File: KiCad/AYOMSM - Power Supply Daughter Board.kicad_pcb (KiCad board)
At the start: 2 copper layers, 97.8 x 47.3 mm, 21 parts

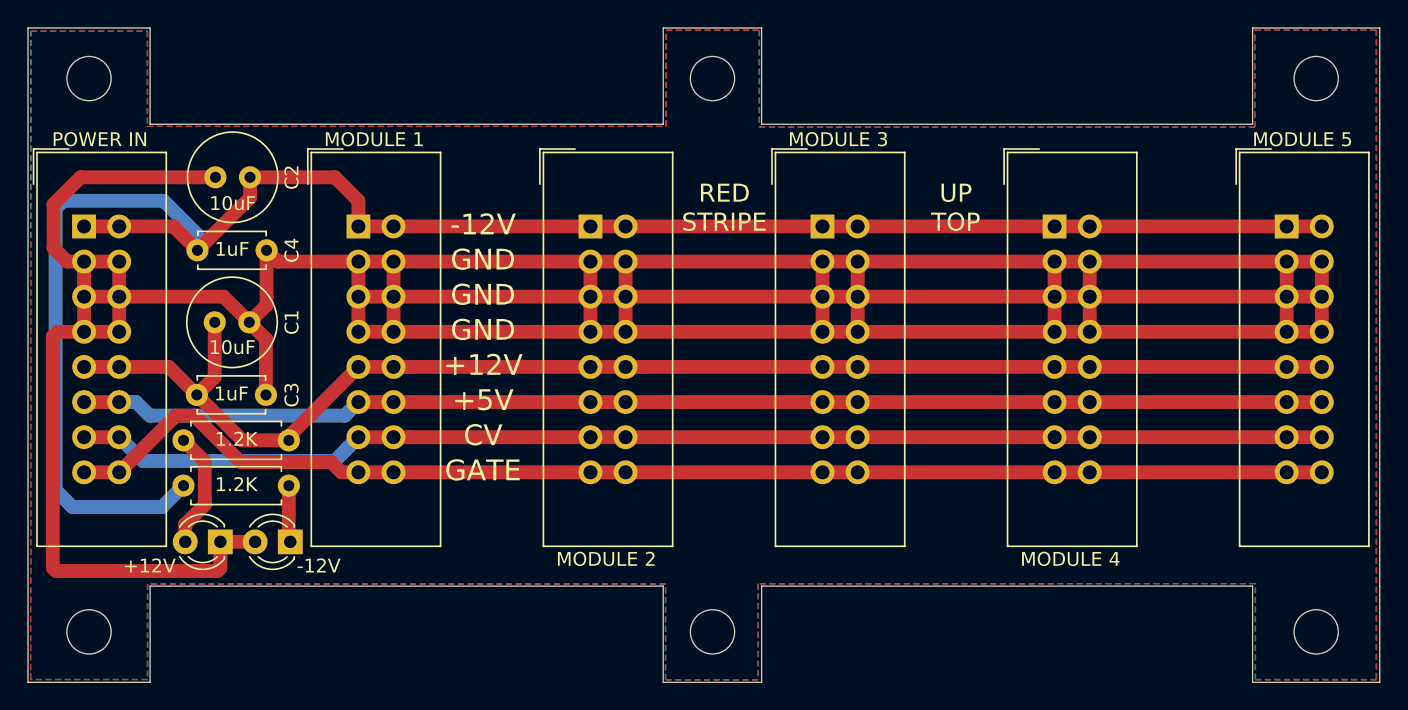
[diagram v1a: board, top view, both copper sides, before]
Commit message: Added 10-pin Power-In connector, updated layout
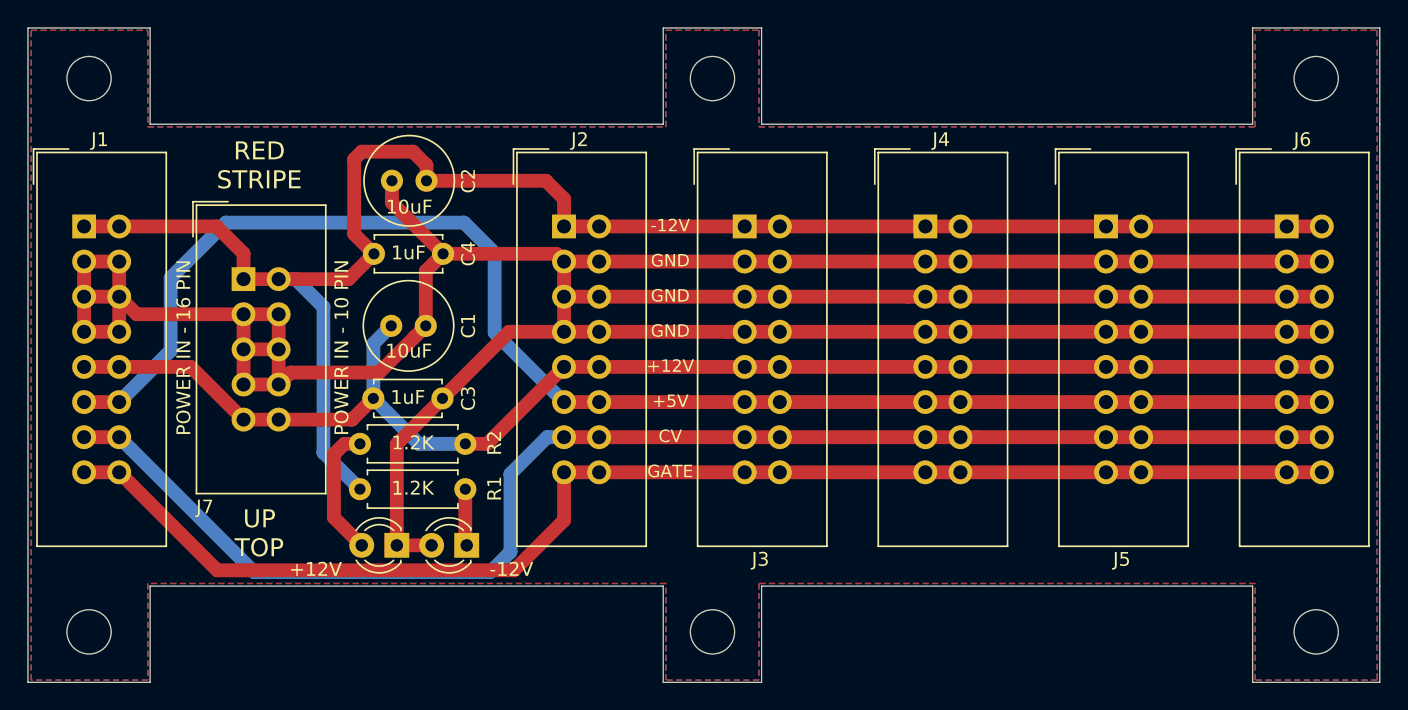
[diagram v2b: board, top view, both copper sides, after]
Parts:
- added J7: PWR_IN_10, Connector_IDC:IDC-Header_2x05_P2.54mm_Vertical, F.Cu at (124.6, 72.5)
- J1: renamed from POWER IN
- J2: renamed from MODULE 1
- J3: renamed from MODULE 2
- J4: renamed from MODULE 3
- J5: renamed from MODULE 4
- J6: renamed from MODULE 5
- moved G*** 35.9 mm to (123.3, 84.6)
- moved J2 14.9 mm to (147.8, 68.7)
- moved R1 12.8 mm to (140.6, 87.7)
- moved R2 12.8 mm to (133.0, 84.5)
- moved +12V 12.8 mm to (135.7, 91.8)
- moved -12V 12.8 mm to (140.7, 91.8)
- moved C2 12.8 mm to (135.3, 65.4)
- moved C3 12.8 mm to (134.0, 81.2)
- moved C4 12.8 mm to (139.0, 70.7)
- moved C1 12.8 mm to (135.3, 75.9)
- moved J3 11.2 mm to (160.8, 68.7)
- moved J4 7.44 mm to (173.9, 68.7)
- moved J5 3.72 mm to (187.0, 68.7)
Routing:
- net GND: track 360.4 -> 273.8 mm
- net /5V: track 90.3 -> 106.7 mm
- net -12V: track 139.2 -> 124.4 mm
- net /CV: track 90.9 -> 100.9 mm
- net /GATE: track 92.9 -> 97.4 mm
- net +12V: track 99.9 -> 101.2 mm
- net Net-(D1-Pad2): track 8.57 -> 9.61 mm
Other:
- board text added: "POWER IN - 10 PIN"
- board text added: "POWER IN - 16 PIN"
- board text added: "R1"
- board text added: "R2"
- board text added: "Shapetaker - Power Supply Daughter Board (Power Bus - Rev 1.1)"
- board text removed: "Shapetaker - Power Supply Daughter Board (Power Bus - Rev 1.0)"

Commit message: Updated BOM, ordering information, updated silkscreen, added README
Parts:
- renumbered +12V to D1, -12V to D2
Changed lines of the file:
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@@
   (general
     (thickness 1.6)
-    (drawings 37)
+    (drawings 41)
     (tracks 167)
     (zones 0)
@@
   )
   (page A4)
+  (title_block
+    (title "Power Supply Bus")
+    (date 2020-07-25)
+    (rev 1.0)
+    (company Shapetaker)
+  )
   (layers
     (0 F.Cu signal)
@@
     (descr "LED, diameter 3.0mm, 2 pins")
     (tags "LED diameter 3.0mm 2 pins")
-    (fp_text reference +12V (at 5.8801 -1.7399) (layer F.SilkS)
+    (fp_text reference D1 (at 4.6736 -2.1209) (layer F.SilkS)
       (effects (font (size 1 1) (thickness 0.15)))
     )
@@
     (descr "LED, diameter 3.0mm, 2 pins")
     (tags "LED diameter 3.0mm 2 pins")
-    (fp_text reference -12V (at -3.2258 -1.7399) (layer F.SilkS)
+    (fp_text reference D2 (at -2.2098 -2.1209) (layer F.SilkS)
       (effects (font (size 1 1) (thickness 0.15)))
     )
@@
     )
   )
-  (gr_text R2 (at 142.748 84.3915 90) (layer F.SilkS)
+  (gr_text -12V (at 143.006 90.551 270) (layer F.SilkS)
     (effects (font (size 1 1) (thickness 0.15)))
   )
-  (gr_text R1 (at 142.748 87.6935 90) (layer F.SilkS)
+  (gr_text +12V (at 131.0045 90.551 270) (layer F.SilkS)
     (effects (font (size 1 1) (thickness 0.15)))
   )
-  (gr_text "POWER IN - 10 PIN" (at 131.699 77.497401 90) (layer F.SilkS)
+  (dimension 47.3202 (width 0.15) (layer Dwgs.User)
+    (gr_text "47.320 mm" (at 103.7925 78.0415 270) (layer Dwgs.User)
+      (effects (font (size 1 1) (thickness 0.15)))
+    )
+    (feature1 (pts (xy 109 101.7016) (xy 104.506079 101.7016)))
+    (feature2 (pts (xy 109 54.3814) (xy 104.506079 54.3814)))
+    (crossbar (pts (xy 105.0925 54.3814) (xy 105.0925 101.7016)))
+    (arrow1a (pts (xy 105.0925 101.7016) (xy 104.506079 100.575096)))
+    (arrow1b (pts (xy 105.0925 101.7016) (xy 105.678921 100.575096)))
+    (arrow2a (pts (xy 105.0925 54.3814) (xy 104.506079 55.507904)))
+    (arrow2b (pts (xy 105.0925 54.3814) (xy 105.678921 55.507904)))
+  )
+  (dimension 97.756 (width 0.15) (layer Dwgs.User)
+    (gr_text "97.756 mm" (at 157.878 50.135) (layer Dwgs.User)
+      (effects (font (size 1 1) (thickness 0.15)))
+    )
+    (feature1 (pts (xy 206.756 54.3814) (xy 206.756 50.848579)))
+    (feature2 (pts (xy 109 54.3814) (xy 109 50.848579)))
+    (crossbar (pts (xy 109 51.435) (xy 206.756 51.435)))
+    (arrow1a (pts (xy 206.756 51.435) (xy 205.629496 52.021421)))
+    (arrow1b (pts (xy 206.756 51.435) (xy 205.629496 50.848579)))
+    (arrow2a (pts (xy 109 51.435) (xy 110.126504 52.021421)))
+    (arrow2b (pts (xy 109 51.435) (xy 110.126504 50.848579)))
+  )
+  (gr_text R2 (at 142.748 83.98119 90) (layer F.SilkS)
     (effects (font (size 1 1) (thickness 0.15)))
   )
+  (gr_text R1 (at 142.748 87.25779 90) (layer F.SilkS)
+    (effects (font (size 1 1) (thickness 0.15)))
+  )
+  (gr_text "POWER IN - 10 PIN" (at 131.3815 77.497401 90) (layer F.SilkS)
+    (effects (font (size 1 1) (thickness 0.15)))
+  )

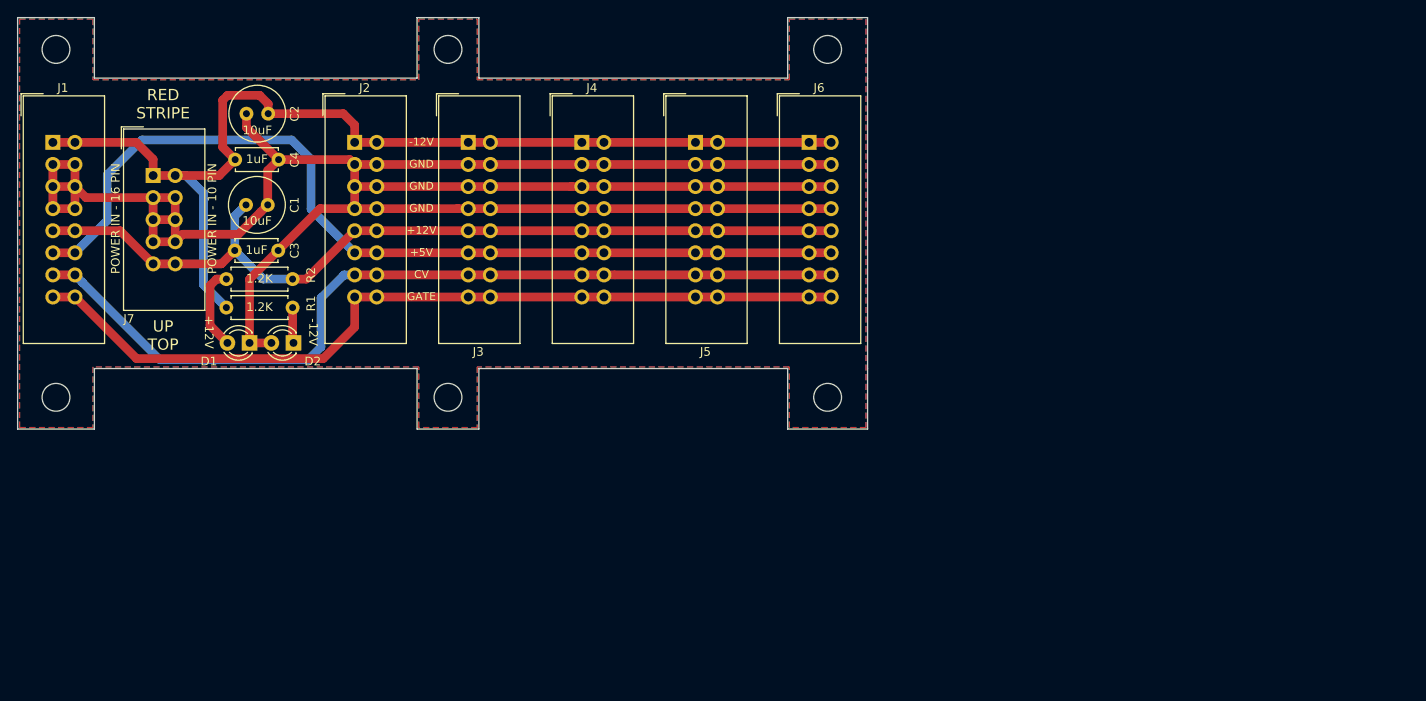
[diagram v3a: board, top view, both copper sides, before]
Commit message: Updated silkscreen
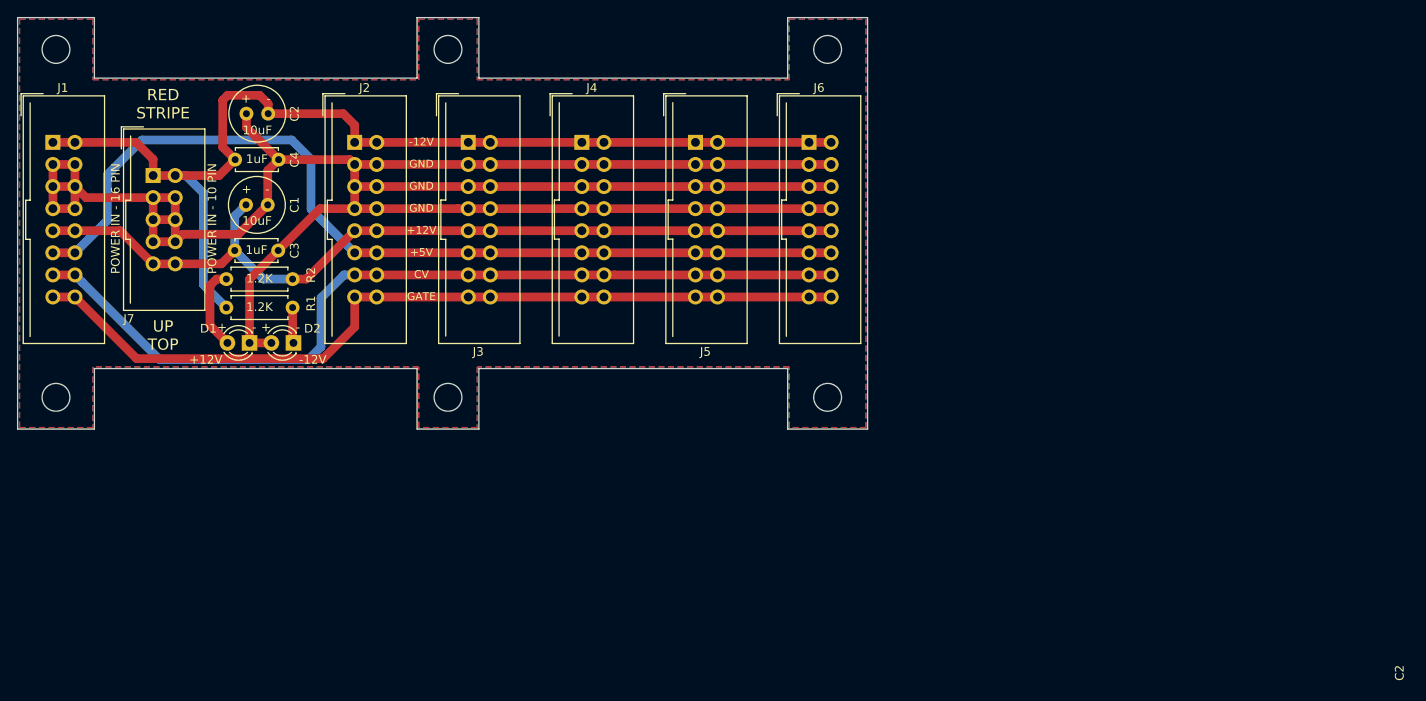
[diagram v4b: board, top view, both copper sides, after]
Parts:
- added ?: , , F.Cu at (132.5, 65.0)
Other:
- board text added: "+"
- board text added: "-"
- board text added: "Shapetaker - Power Supply Daughter Board (Power Bus - Rev 1.2)"
- board text removed: "Shapetaker - Power Supply Daughter Board (Power Bus - Rev 1.1)"
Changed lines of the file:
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@@
   (general
     (thickness 1.6)
-    (drawings 41)
+    (drawings 84)
     (tracks 167)
     (zones 0)
-    (modules 22)
+    (modules 23)
     (nets 9)
   )
@@
   (title_block
     (title "Power Supply Bus")
-    (date 2020-07-25)
-    (rev 1.0)
+    (date 2020-08-08)
+    (rev 1.2)
     (company Shapetaker)
   )
@@
     (add_net "Net-(D1-Pad2)")
     (add_net "Net-(D2-Pad1)")
+  )
+  (module "" (layer F.Cu)
+    (at 132.461 64.9986)
+    (fp_text reference "" (at 135.3185 65.4304) (layer F.SilkS)
+      (effects (font (size 1.27 1.27) (thickness 0.15)))
+    )
+    (fp_text value "" (at 135.3185 65.4304) (layer F.SilkS)
+      (effects (font (size 1.27 1.27) (thickness 0.15)))
+    )
+    (fp_text user C2 (at 135.4836 64.744601 90) (layer F.SilkS)
+      (effects (font (size 1 1) (thickness 0.15)))
+    )
   )
   (module Capacitor_THT:C_Radial_D6.3mm_H11.0mm_P2.50mm (layer F.Cu)
@@
     (descr "LED, diameter 3.0mm, 2 pins")
     (tags "LED diameter 3.0mm 2 pins")
-    (fp_text reference D1 (at 4.6736 -2.1209) (layer F.SilkS)
+    (fp_text reference D1 (at 4.7371 1.651) (layer F.SilkS)
       (effects (font (size 1 1) (thickness 0.15)))
     )
@@
     (descr "LED, diameter 3.0mm, 2 pins")
     (tags "LED diameter 3.0mm 2 pins")
-    (fp_text reference D2 (at -2.2098 -2.1209) (layer F.SilkS)
+    (fp_text reference D2 (at -2.1717 1.651) (layer F.SilkS)
       (effects (font (size 1 1) (thickness 0.15)))
     )
@@
     )
   )
-  (gr_text -12V (at 143.006 90.551 270) (layer F.SilkS)
+  (gr_line (start 197.4088 79.8576) (end 197.4088 91.0336) (layer F.SilkS) (width 0.12))
+  (gr_line (start 196.8754 79.8576) (end 197.4088 79.8576) (layer F.SilkS) (width 0.12))
+  (gr_line (start 196.8754 75.3618) (end 196.8754 79.8576) (layer F.SilkS) (width 0.12))
+  (gr_line (start 197.4088 75.3618) (end 196.8754 75.3618) (layer F.SilkS) (width 0.12))
+  (gr_line (start 197.4088 64.1858) (end 197.4088 75.3618) (layer F.SilkS) (width 0.12))
+  (gr_line (start 184.3532 79.8576) (end 184.3532 91.059) (layer F.SilkS) (width 0.12))
+  (gr_line (start 183.8198 79.8576) (end 184.3532 79.8576) (layer F.SilkS) (width 0.12))
+  (gr_line (start 183.8198 75.3618) (end 183.8198 79.8576) (layer F.SilkS) (width 0.12))
+  (gr_line (start 184.3532 75.3618) (end 183.8198 75.3618) (layer F.SilkS) (width 0.12))
+  (gr_line (start 184.3532 64.1604) (end 184.3532 75.3618) (layer F.SilkS) (width 0.12))
+  (gr_line (start 171.2722 79.8576) (end 171.2722 91.0082) (layer F.SilkS) (width 0.12))
+  (gr_line (start 170.7388 79.8576) (end 171.2722 79.8576) (layer F.SilkS) (width 0.12))
+  (gr_line (start 170.7388 75.3618) (end 170.7388 79.8576) (layer F.SilkS) (width 0.12))
+  (gr_line (start 171.2976 75.3618) (end 170.7388 75.3618) (layer F.SilkS) (width 0.12))
+  (gr_line (start 171.2976 64.1604) (end 171.2976 75.3618) (layer F.SilkS) (width 0.12))
+  (gr_line (start 158.242 79.883) (end 158.242 91.0082) (layer F.SilkS) (width 0.12))
+  (gr_line (start 157.6832 79.883) (end 158.242 79.883) (layer F.SilkS) (width 0.12))
+  (gr_line (start 157.6832 75.3618) (end 157.6832 79.883) (layer F.SilkS) (width 0.12))
+  (gr_line (start 158.242 75.3618) (end 157.6832 75.3618) (layer F.SilkS) (width 0.12))
+  (gr_line (start 158.242 64.1858) (end 158.242 75.3618) (layer F.SilkS) (width 0.12))
+  (gr_line (start 145.161 79.883) (end 145.161 91.0336) (layer F.SilkS) (width 0.12))
+  (gr_line (start 144.6276 79.883) (end 145.161 79.883) (layer F.SilkS) (width 0.12))
+  (gr_line (start 144.6276 75.3872) (end 144.6276 79.883) (layer F.SilkS) (width 0.12))
+  (gr_line (start 145.161 75.3872) (end 144.6276 75.3872) (layer F.SilkS) (width 0.12))
+  (gr_line (start 145.161 64.1858) (end 145.161 75.3872) (layer F.SilkS) (width 0.12))
+  (gr_line (start 121.9708 79.883) (end 121.9708 87.2236) (layer F.SilkS) (width 0.12))
+  (gr_line (start 121.4374 79.883) (end 121.9708 79.883) (layer F.SilkS) (width 0.12))
+  (gr_line (start 121.4374 75.3872) (end 121.4374 79.883) (layer F.SilkS) (width 0.12))
+  (gr_line (start 121.9962 75.3872) (end 121.4374 75.3872) (layer F.SilkS) (width 0.12))
+  (gr_line (start 121.9962 67.9958) (end 121.9962 75.3872) (layer F.SilkS) (width 0.12))
+  (gr_line (start 110.4392 79.883) (end 110.4392 91.059) (layer F.SilkS) (width 0.12))
+  (gr_line (start 109.9312 79.883) (end 110.4392 79.883) (layer F.SilkS) (width 0.12))
+  (gr_line (start 109.9312 75.3872) (end 109.9312 79.883) (layer F.SilkS) (width 0.12))
+  (gr_line (start 110.4392 75.3872) (end 109.9312 75.3872) (layer F.SilkS) (width 0.12))
+  (gr_line (start 110.4392 64.1858) (end 110.4392 75.3872) (layer F.SilkS) (width 0.12))
+  (gr_text - (at 141.2494 89.9922) (layer F.SilkS)
     (effects (font (size 1 1) (thickness 0.15)))
   )
-  (gr_text +12V (at 131.0045 90.551 270) (layer F.SilkS)
+  (gr_text + (at 137.5664 89.9922) (layer F.SilkS)
+    (effects (font (size 1 1) (thickness 0.15)))
+  )
+  (gr_text - (at 136.2202 89.9922) (layer F.SilkS)
+    (effects (font (size 1 1) (thickness 0.15)))
+  )
+  (gr_text + (at 132.5118 89.9922) (layer F.SilkS)
+    (effects (font (size 1 1) (thickness 0.15)))
+  )
+  (gr_text - (at 137.7188 74.1172) (layer F.SilkS)
+    (effects (font (size 1 1) (thickness 0.15)))
+  )
+  (gr_text + (at 135.3312 74.1172) (layer F.SilkS)
+    (effects (font (size 1 1) (thickness 0.15)))
+  )
+  (gr_text - (at 137.8712 63.7032) (layer F.SilkS)
+    (effects (font (size 1 1) (thickness 0.15)))
+  )
+  (gr_text + (at 135.2804 63.7032) (layer F.SilkS)
+    (effects (font (size 1 1) (thickness 0.15)))
+  )
+  (gr_text -12V (at 142.9512 93.726) (layer F.SilkS)
+    (effects (font (size 1 1) (thickness 0.15)))
+  )
+  (gr_text +12V (at 130.6576 93.726) (layer F.SilkS)
     (effects (font (size 1 1) (thickness 0.15)))
   )
@@
     (effects (font (size 0.9 0.9) (thickness 0.15)))
   )
-  (gr_text "Shapetaker - Power Supply Daughter Board (Power Bus - Rev 1.1)" (at 171.831 93.218) (layer B.SilkS)
+  (gr_text "Shapetaker - Power Supply Daughter Board (Power Bus - Rev 1.2)" (at 171.831 93.218) (layer B.SilkS)
     (effects (font (size 1 1) (thickness 0.15)) (justify mirror))
   )
